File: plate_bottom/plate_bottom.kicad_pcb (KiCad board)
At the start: 2 copper layers, 178.4 x 118.1 mm, 15 parts

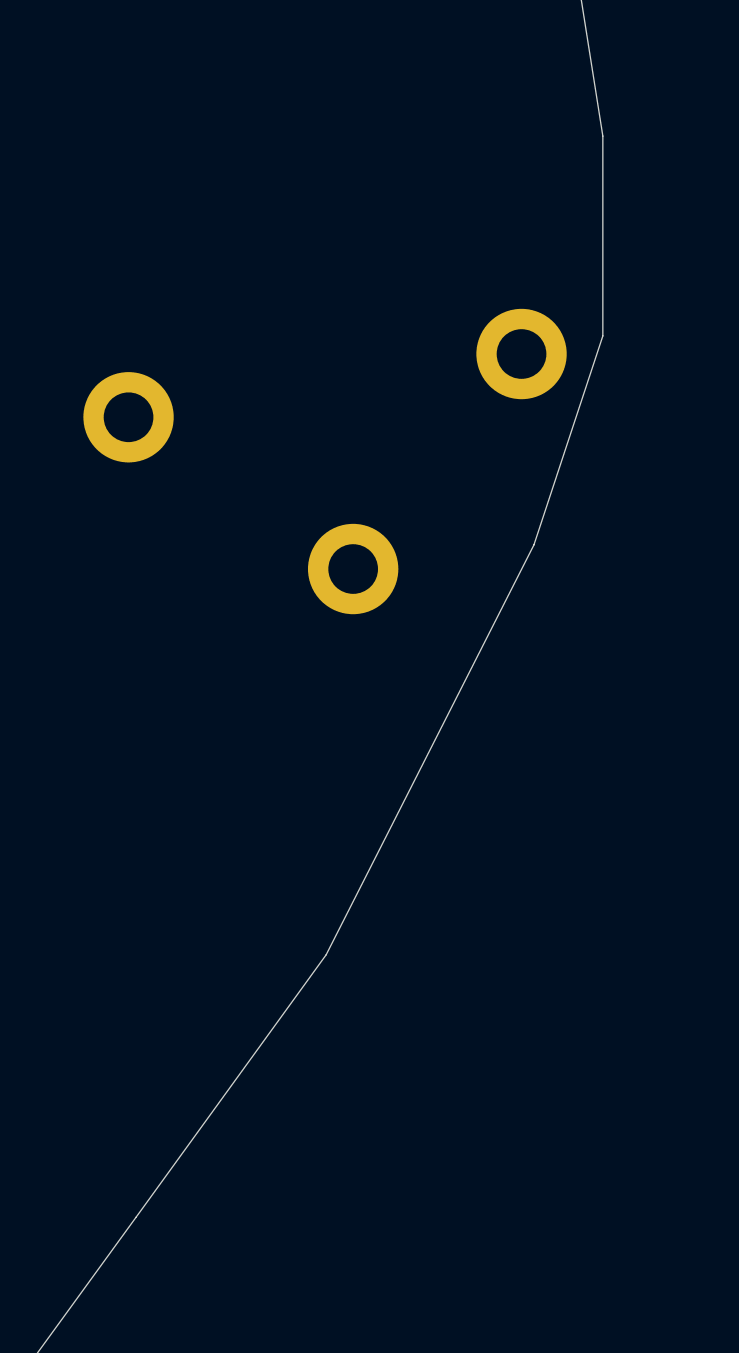
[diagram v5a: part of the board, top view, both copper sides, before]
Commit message: Changed the shape of the right edge.
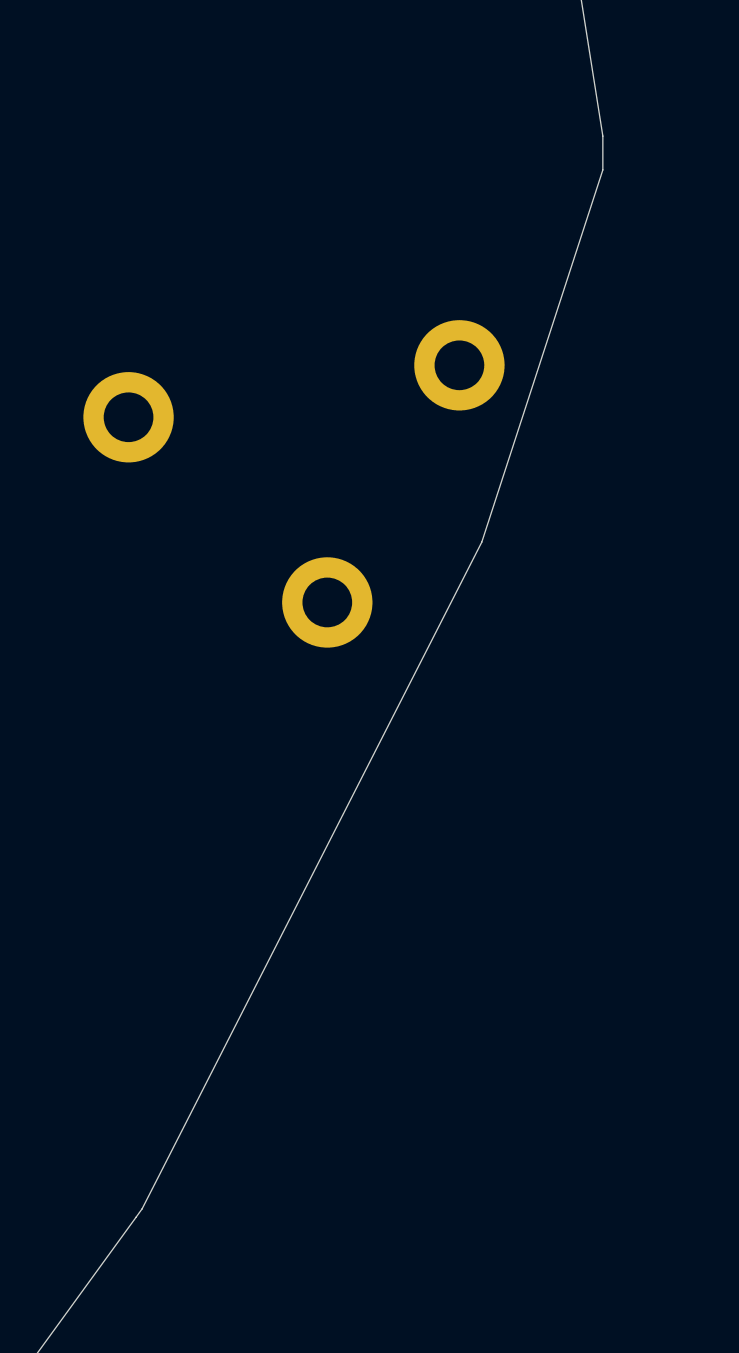
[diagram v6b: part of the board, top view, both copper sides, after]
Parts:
- moved H15 2.80 mm to (248.6, 96.3)
- moved HM3 1.87 mm to (242.8, 106.8)
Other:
- outline, holes or cut-outs redrawn
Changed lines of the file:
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@@
   (general
     (thickness 1.6)
-    (drawings 123)
+    (drawings 122)
     (tracks 0)
     (zones 0)
@@
   )
   (module used_footprints:M2_HOLE_PCB (layer F.Cu)
+    (at 248.6 96.35 9)
+    (fp_text reference H15 (at 0 2.7 9) (layer F.SilkS) hide
+      (effects (font (size 1 1) (thickness 0.15)))
+    )
+    (fp_text value MountingHole (at 0 -2.6 9) (layer F.Fab) hide
+      (effects (font (size 1 1) (thickness 0.15)))
+    )
+    (pad "" thru_hole circle (at 0 0 9) (size 4 4) (drill 2.2) (layers *.Cu *.Mask))
+  )
+  (module used_footprints:M2_HOLE_PCB (layer F.Cu)
+    (at 242.75 106.85)
+    (fp_text reference HM3 (at 0 2.7) (layer F.SilkS) hide
+      (effects (font (size 1 1) (thickness 0.15)))
+    )
+    (fp_text value CaseHole (at 0 -2.6) (layer F.Fab) hide
+      (effects (font (size 1 1) (thickness 0.15)))
+    )
+    (pad "" thru_hole circle (at 0 0) (size 4 4) (drill 2.2) (layers *.Cu *.Mask))
+  )
+  (module used_footprints:M2_HOLE_PCB (layer F.Cu)
     (at 215.3 123.325)
     (fp_text reference HM1 (at 0 2.7) (layer F.SilkS) hide
@@
   )
   (module used_footprints:M2_HOLE_PCB (layer F.Cu)
-    (at 251.35 95.85 9)
-    (fp_text reference H15 (at 0 2.7 9) (layer F.SilkS) hide
-      (effects (font (size 1 1) (thickness 0.15)))
-    )
-    (fp_text value MountingHole (at 0 -2.6 9) (layer F.Fab) hide
-      (effects (font (size 1 1) (thickness 0.15)))
-    )
-    (pad "" thru_hole circle (at 0 0 9) (size 4 4) (drill 2.2) (layers *.Cu *.Mask))
-  )
-  (module used_footprints:M2_HOLE_PCB (layer F.Cu)
     (at 152.65 68.5)
     (fp_text reference HM11 (at 0 2.7) (layer F.SilkS) hide
@@
   )
   (module used_footprints:M2_HOLE_PCB (layer F.Cu)
-    (at 243.895 105.37)
-    (fp_text reference HM3 (at 0 2.7) (layer F.SilkS) hide
-      (effects (font (size 1 1) (thickness 0.15)))
-    )
-    (fp_text value CaseHole (at 0 -2.6) (layer F.Fab) hide
-      (effects (font (size 1 1) (thickness 0.15)))
-    )
-    (pad "" thru_hole circle (at 0 0) (size 4 4) (drill 2.2) (layers *.Cu *.Mask))
-  )
-  (module used_footprints:M2_HOLE_PCB (layer F.Cu)
     (at 114.5 98.6)
     (fp_text reference HM6 (at 0 2.7) (layer F.SilkS) hide
@@
     (pad "" np_thru_hole circle (at 0 0.55) (size 2.2 2.2) (drill 2.2) (layers *.Cu *.Mask))
   )
-  (gr_line (start 254.95 99.8) (end 254.95 95.65) (layer Dwgs.User) (width 0.15))
+  (gr_line (start 234.283043 134.070973) (end 234.55 133.7) (layer Edge.Cuts) (width 0.05))
+  (gr_line (start 254.95 87.7) (end 249.59 104.18) (layer Edge.Cuts) (width 0.05))
+  (gr_line (start 254.95 86.2) (end 254.95 87.7) (layer Edge.Cuts) (width 0.05))
+  (gr_line (start 249.59 104.18) (end 234.55 133.7) (layer Edge.Cuts) (width 0.05))
   (gr_line (start 153.75 148.65) (end 222.6 148.65) (layer Dwgs.User) (width 0.15))
   (dimension 118.1 (width 0.15) (layer Dwgs.User)
@@
   (gr_line (start 247.677579 53.038559) (end 227.4 56.25) (layer Edge.Cuts) (width 0.05))
   (gr_line (start 249.965825 54.701067) (end 254.95 86.2) (layer Edge.Cuts) (width 0.05))
-  (gr_line (start 254.95 95.05) (end 251.9 104.3) (layer Edge.Cuts) (width 0.05))
-  (gr_line (start 251.9 104.3) (end 242.7 122.45) (layer Edge.Cuts) (width 0.05))
   (gr_arc (start 247.990448 55.013936) (end 249.965825 54.701067) (angle -90) (layer Edge.Cuts) (width 0.05))
-  (gr_line (start 254.95 86.2) (end 254.95 95.05) (layer Edge.Cuts) (width 0.05))
-  (gr_line (start 242.7 122.45) (end 234.283043 134.070973) (layer Edge.Cuts) (width 0.05))
   (gr_line (start 234.283043 134.070973) (end 223.996802 148.22877) (layer Edge.Cuts) (width 0.05))
   (gr_line (start 96.6 117.55) (end 139.35 117.55) (layer Edge.Cuts) (width 0.05))

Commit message: Multiple fixes...
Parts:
- removed H13: MountingHole, used_footprints:M2_HOLE_PCB
- moved H16 8.00 mm to (222.2, 75.7)
- moved HM12 4.25 mm to (228.0, 74.8)
- moved HM1 2.22 mm to (217.5, 123.3)
- moved HM4 2.21 mm to (166.4, 113.7)
- moved H15 2.10 mm to (246.7, 97.2)
- moved HM3 0.78 mm to (242.6, 107.6)
- moved HM5 0.55 mm to (95.5, 96.2)
- moved HM6 0.05 mm to (114.5, 98.7)
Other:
- outline, holes or cut-outs redrawn

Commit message: top + bottom plates
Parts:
- removed H15: MountingHole, used_footprints:M2_HOLE_PCB
- removed HM12: CaseHole, used_footprints:M2_HOLE_PCB
- moved HM4 8.89 mm to (175.1, 115.3)
- moved HM7 4.19 mm to (110.4, 59.3), turned to 4.5 degrees
- moved HM1 3.64 mm to (221.2, 123.1)
- moved H16 3.09 mm to (222.2, 72.6)
- moved HM8 2.68 mm to (111.9, 78.9), turned to 4.5 degrees
- moved HM5 1.45 mm to (94.2, 96.9), turned to 4.5 degrees
- moved HM6 1.33 mm to (113.4, 97.9), turned to 4.5 degrees
- moved HM3 1.02 mm to (243.5, 108.1)
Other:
- board size 178.4 x 118.1 mm -> 180.6 x 117.9 mm
